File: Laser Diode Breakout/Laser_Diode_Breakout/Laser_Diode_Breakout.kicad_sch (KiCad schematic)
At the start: 3 parts, among them J1 Conn_01x03_Pin

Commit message: generated BOM
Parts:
- D1: value LED -> 785nm Laser Diode
- D2: value LED -> 520nm Laser Diode
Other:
- moved on the sheet: D1, D2, J1

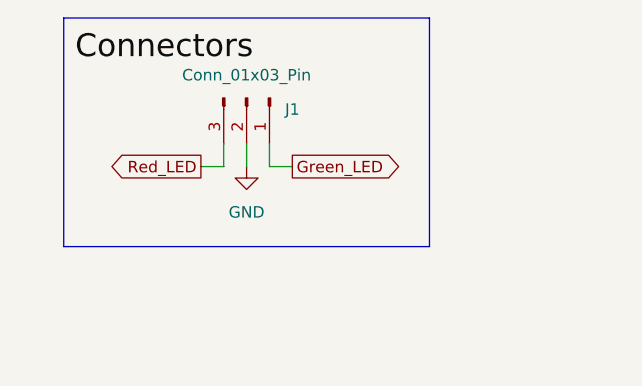
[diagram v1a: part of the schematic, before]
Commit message: fix: switched connectors to Molex
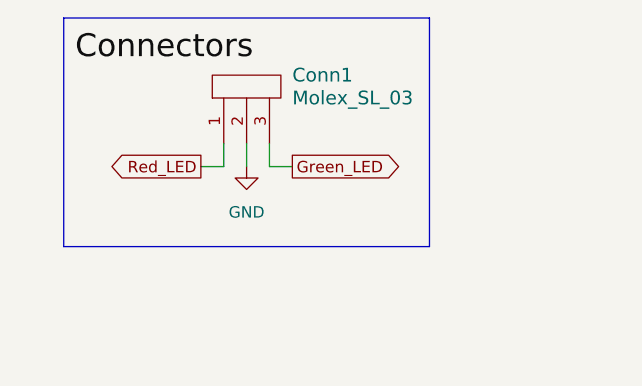
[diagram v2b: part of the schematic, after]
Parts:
- removed J1: Conn_01x03_Pin, symbol Connector:Conn_01x03_Pin
- added Conn1: Molex_SL_03, symbol MRDT_Connectors:Molex_SL_03
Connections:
- net GND: now also Conn1.2
- net Green_LED: now also Conn1.3
- net Red_LED: now also Conn1.1
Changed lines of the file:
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@@
+    )
+  )
+  (symbol (lib_id "MRDT_Connectors:Molex_SL_03") (at 57.15 26.67 90) (unit 1)
+    (in_bom yes) (on_board yes) (dnp no) (fields_autoplaced)
+    (property "Reference" "Conn1" (at 58.42 24.13 90)
+      (effects (font (size 1.524 1.524)) (justify right))
+    )
+    (property "Value" "Molex_SL_03" (at 58.42 26.67 90)
+      (effects (font (size 1.524 1.524)) (justify right))
+    )
+    (property "Footprint" "" (at 57.15 26.67 0)
+      (effects (font (size 1.524 1.524)) hide)
+    )
+    (property "Datasheet" "" (at 57.15 26.67 0)
+      (effects (font (size 1.524 1.524)) hide)
+    )
+    (pin "1")
+    (pin "2")
+    (pin "3")
+    (instances
+      (project "Laser_Diode_Breakout"
+        (path "/c855c228-4e5d-4dfd-9922-c2d1c9f93d6f"
+          (reference "Conn1") (unit 1)
+        )
+      )
     )
   )
@@
         )
       )
-    )
-  )
-  (symbol (lib_id "Connector:Conn_01x03_Pin") (at 53.34 26.67 270) (unit 1)
-    (in_bom yes) (on_board yes) (dnp no)
-    (property "Reference" "J1" (at 58.42 27.94 90)
-      (effects (font (size 1.27 1.27)))
-    )
-    (property "Value" "Conn_01x03_Pin" (at 53.34 24.13 90)
-      (effects (font (size 1.27 1.27)))
-    )
-    (property "Footprint" "" (at 53.34 26.67 0)
-      (effects (font (size 1.27 1.27)) hide)
-    )
-    (property "Datasheet" "~" (at 53.34 26.67 0)
-      (effects (font (size 1.27 1.27)) hide)
-    )
-    (pin "1")
-    (pin "2")
-    (pin "3")
-    (instances
-      (project "Laser_Diode_Breakout"
-        (path "/c855c228-4e5d-4dfd-9922-c2d1c9f93d6f"
-          (reference "J1") (unit 1)
-        )
-      )

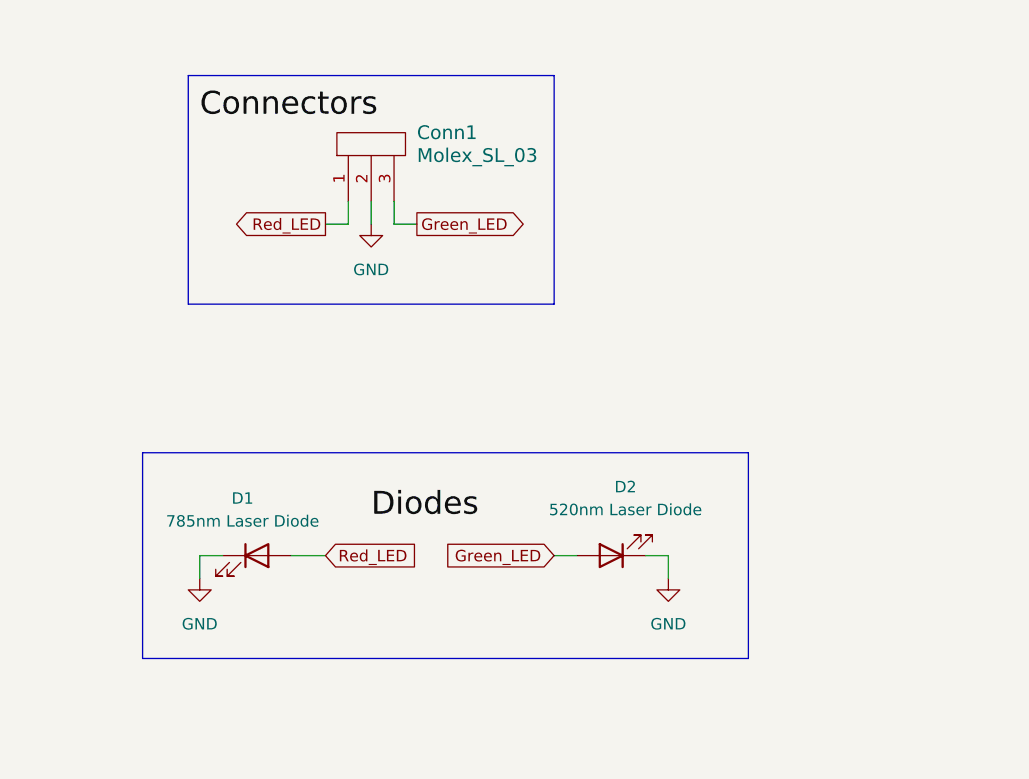
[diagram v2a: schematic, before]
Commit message: fix: replaced net labels with text
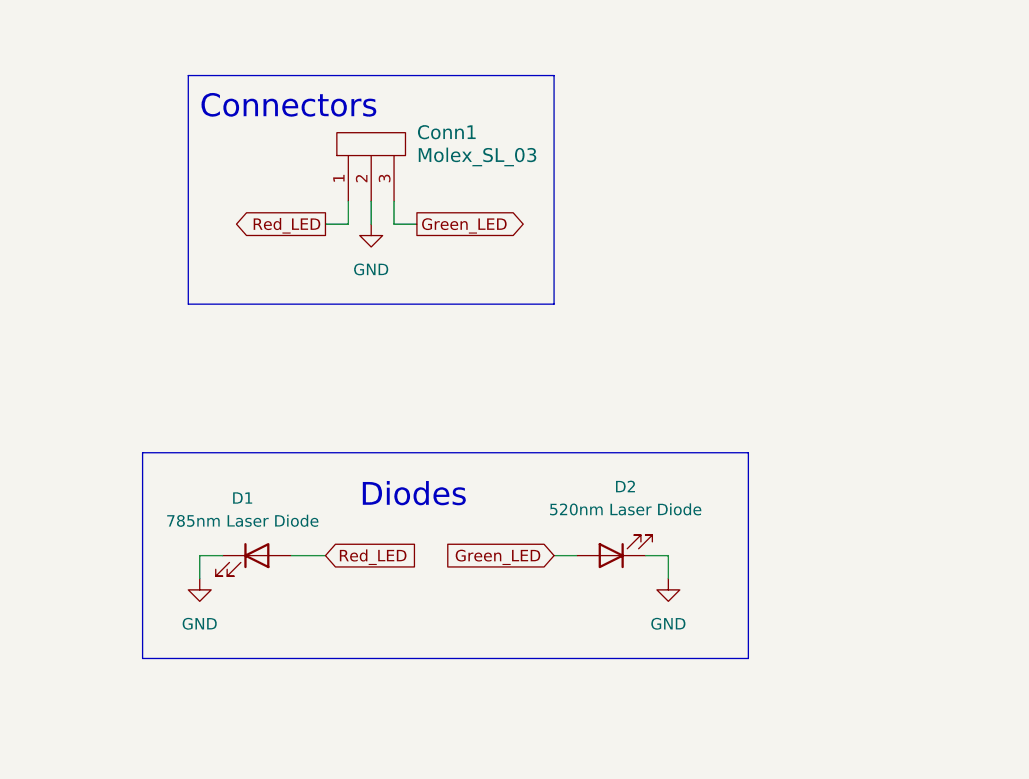
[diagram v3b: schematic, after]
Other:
- note added: "Connectors"
- note added: "Diodes"
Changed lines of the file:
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@@
     (stroke (width 0) (type default))
   )
-  (label "Diodes" (at 53.34 67.31 0) (fields_autoplaced)
+  (text "Connectors" (at 34.29 22.86 0)
     (effects (font (size 2.54 2.54)) (justify left bottom))
   )
-  (label "Connectors" (at 34.29 22.86 0) (fields_autoplaced)
+  (text "Diodes" (at 52.07 66.04 0)
     (effects (font (size 2.54 2.54)) (justify left bottom))
   )

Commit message: misc schematic review changes
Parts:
- added R1: 17, symbol Device:R
- added R2: 24, symbol Device:R
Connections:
- net Green_LED: now also R1.1; no longer D2.2 (A)
- net Red_LED: now also R2.2; no longer D1.2 (A)
- new net: D2.2 (A), R1.2
- new net: D1.2 (A), R2.1
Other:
- moved on the sheet: D2
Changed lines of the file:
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@@
     (stroke (width 0) (type default))
   )
-  (polyline (pts (xy 95.25 82.55) (xy 27.94 82.55))
+  (polyline (pts (xy 124.46 83.82) (xy 27.94 83.82))
     (stroke (width 0) (type default))
   )
@@
     (stroke (width 0) (type default))
   )
-  (polyline (pts (xy 95.25 59.69) (xy 95.25 82.55))
+  (polyline (pts (xy 124.46 60.96) (xy 124.46 83.82))
     (stroke (width 0) (type default))
   )
@@
     (stroke (width 0) (type default))
   )
-  (polyline (pts (xy 27.94 59.69) (xy 95.25 59.69))
+  (polyline (pts (xy 27.94 60.96) (xy 124.46 60.96))
     (stroke (width 0) (type default))
   )
@@
     (stroke (width 0) (type default))
   )
-  (wire (pts (xy 44.45 71.12) (xy 48.26 71.12))
+  (wire (pts (xy 58.42 71.12) (xy 62.23 71.12))
+    (stroke (width 0) (type default))
+  )
+  (wire (pts (xy 44.45 71.12) (xy 50.8 71.12))
     (stroke (width 0) (type default))
   )
@@
     (stroke (width 0) (type default))
   )
-  (wire (pts (xy 86.36 71.12) (xy 86.36 73.66))
-    (stroke (width 0) (type default))
-  )
-  (wire (pts (xy 73.66 71.12) (xy 76.2 71.12))
+  (wire (pts (xy 116.84 72.39) (xy 116.84 74.93))
+    (stroke (width 0) (type default))
+  )
+  (wire (pts (xy 92.71 72.39) (xy 95.25 72.39))
     (stroke (width 0) (type default))
   )
@@
     (stroke (width 0) (type default))
   )
+  (wire (pts (xy 102.87 72.39) (xy 106.68 72.39))
+    (stroke (width 0) (type default))
+  )
   (wire (pts (xy 55.88 31.75) (xy 55.88 34.29))
     (stroke (width 0) (type default))
@@
     (stroke (width 0) (type default))
   )
-  (wire (pts (xy 83.82 71.12) (xy 86.36 71.12))
+  (wire (pts (xy 114.3 72.39) (xy 116.84 72.39))
     (stroke (width 0) (type default))
   )
@@
     )
   )
-  (global_label "Red_LED" (shape input) (at 48.26 71.12 0) (fields_autoplaced)
+  (global_label "Red_LED" (shape input) (at 62.23 71.12 0) (fields_autoplaced)
     (effects (font (size 1.27 1.27)) (justify left))
-    (property "Intersheetrefs" "${INTERSHEET_REFS}" (at 59.1675 71.12 0)
+    (property "Intersheetrefs" "${INTERSHEET_REFS}" (at 73.1375 71.12 0)
       (effects (font (size 1.27 1.27)) (justify left) hide)
     )
   )
-  (global_label "Green_LED" (shape input) (at 73.66 71.12 180) (fields_autoplaced)
+  (global_label "Green_LED" (shape input) (at 92.71 72.39 180) (fields_autoplaced)
     (effects (font (size 1.27 1.27)) (justify right))
-    (property "Intersheetrefs" "${INTERSHEET_REFS}" (at 60.8777 71.12 0)
+    (property "Intersheetrefs" "${INTERSHEET_REFS}" (at 79.9277 72.39 0)
       (effects (font (size 1.27 1.27)) (justify right) hide)
     )
   )
-  (symbol (lib_id "Device:LED") (at 80.01 71.12 180) (unit 1)
+  (symbol (lib_id "Device:LED") (at 110.49 72.39 180) (unit 1)
     (in_bom yes) (on_board yes) (dnp no)
-    (property "Reference" "D2" (at 81.5975 63.5 0)
-      (effects (font (size 1.27 1.27)))
-    )
-    (property "Value" "520nm Laser Diode" (at 81.5975 66.04 0)
-      (effects (font (size 1.27 1.27)))
-    )
-    (property "Footprint" "" (at 80.01 71.12 0)
-      (effects (font (size 1.27 1.27)) hide)
-    )
-    (property "Datasheet" "~" (at 80.01 71.12 0)
+    (property "Reference" "D2" (at 112.0775 64.77 0)
+      (effects (font (size 1.27 1.27)))
+    )
+    (property "Value" "520nm Laser Diode" (at 112.0775 67.31 0)
+      (effects (font (size 1.27 1.27)))
+    )
+    (property "Footprint" "" (at 110.49 72.39 0)
+      (effects (font (size 1.27 1.27)) hide)
+    )
+    (property "Datasheet" "~" (at 110.49 72.39 0)
       (effects (font (size 1.27 1.27)) hide)
     )
@@
     )
   )
-  (symbol (lib_id "power:GND") (at 86.36 73.66 0) (unit 1)
-    (in_bom yes) (on_board yes) (dnp no) (fields_autoplaced)
-    (property "Reference" "#PWR01" (at 86.36 80.01 0)
-      (effects (font (size 1.27 1.27)) hide)
-    )
-    (property "Value" "GND" (at 86.36 78.74 0)
-      (effects (font (size 1.27 1.27)))
-    )
-    (property "Footprint" "" (at 86.36 73.66 0)
-      (effects (font (size 1.27 1.27)) hide)
-    )
-    (property "Datasheet" "" (at 86.36 73.66 0)
+  (symbol (lib_id "Device:R") (at 99.06 72.39 90) (unit 1)
+    (in_bom yes) (on_board yes) (dnp no)
+    (property "Reference" "R1" (at 99.06 69.85 90)
+      (effects (font (size 1.27 1.27)))
+    )
+    (property "Value" "17" (at 99.06 72.39 90)
+      (effects (font (size 1.27 1.27)))
+    )
+    (property "Footprint" "" (at 99.06 74.168 90)
+      (effects (font (size 1.27 1.27)) hide)
+    )
+    (property "Datasheet" "~" (at 99.06 72.39 0)
+      (effects (font (size 1.27 1.27)) hide)
+    )
+    (pin "1")
+    (pin "2")
+    (instances
+      (project "Laser_Diode_Breakout"
+        (path "/c855c228-4e5d-4dfd-9922-c2d1c9f93d6f"
+          (reference "R1") (unit 1)
+        )
+      )
+      (project "Raman_Spectrometer_Board"
+        (path "/dd57774e-6364-4f58-a24d-9970470de2f9"
+          (reference "R3") (unit 1)
+        )
+      )
+    )
+  )
+  (symbol (lib_id "power:GND") (at 116.84 74.93 0) (unit 1)
+    (in_bom yes) (on_board yes) (dnp no) (fields_autoplaced)
+    (property "Reference" "#PWR01" (at 116.84 81.28 0)
+      (effects (font (size 1.27 1.27)) hide)
+    )
+    (property "Value" "GND" (at 116.84 80.01 0)
+      (effects (font (size 1.27 1.27)))
+    )
+    (property "Footprint" "" (at 116.84 74.93 0)
+      (effects (font (size 1.27 1.27)) hide)
+    )
+    (property "Datasheet" "" (at 116.84 74.93 0)
       (effects (font (size 1.27 1.27)) hide)
     )
@@
         )
       )
+    )
+  )
+  (symbol (lib_id "Device:R") (at 54.61 71.12 90) (unit 1)
+    (in_bom yes) (on_board yes) (dnp no)
+    (property "Reference" "R2" (at 54.61 68.58 90)
+      (effects (font (size 1.27 1.27)))
+    )
+    (property "Value" "24" (at 54.61 71.12 90)
+      (effects (font (size 1.27 1.27)))
+    )
+    (property "Footprint" "" (at 54.61 72.898 90)
+      (effects (font (size 1.27 1.27)) hide)
+    )
+    (property "Datasheet" "~" (at 54.61 71.12 0)
+      (effects (font (size 1.27 1.27)) hide)
+    )
+    (pin "1")
+    (pin "2")
+    (instances
+      (project "Laser_Diode_Breakout"
+        (path "/c855c228-4e5d-4dfd-9922-c2d1c9f93d6f"
+          (reference "R2") (unit 1)
+        )
+      )
+      (project "Raman_Spectrometer_Board"
+        (path "/dd57774e-6364-4f58-a24d-9970470de2f9"
+          (reference "R4") (unit 1)
+        )
+      )

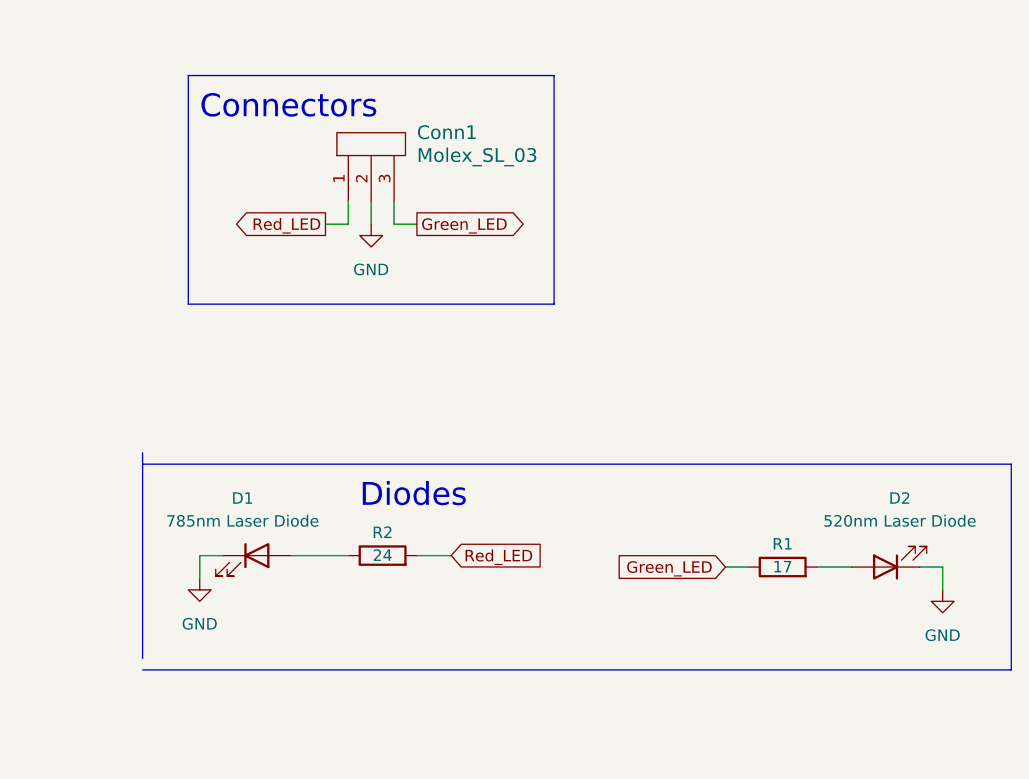
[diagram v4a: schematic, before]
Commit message: fix: use mosfets to control diodes
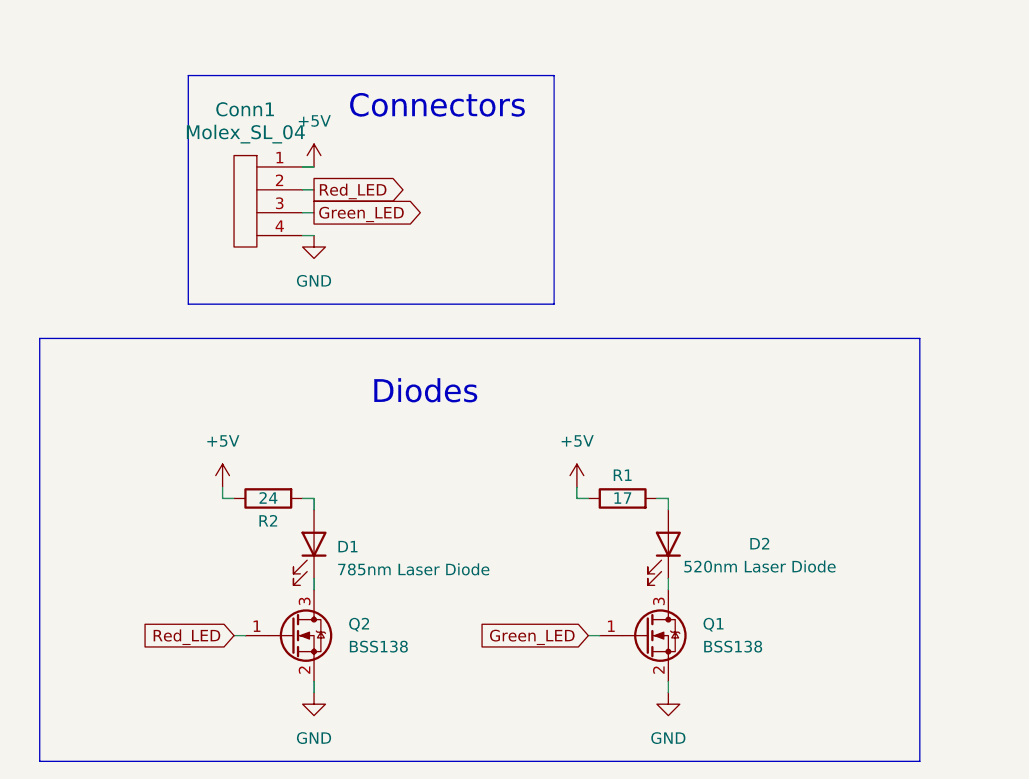
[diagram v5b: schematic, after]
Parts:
- removed Conn1: Molex_SL_03, symbol MRDT_Connectors:Molex_SL_03
- added Conn1: Molex_SL_04, symbol MRDT_Connectors:Molex_SL_04
- added Q1, Q2: BSS138, Package_TO_SOT_SMD:SOT-23, symbol Transistor_FET:BSS138
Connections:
- net GND: now also Conn1.4, Q1.2 (S), Q2.2 (S); no longer D1.1 (K), D2.1 (K)
- net Green_LED: now also Conn1.3, Q1.1 (G); no longer R1.1
- net Red_LED: now also Conn1.2, Q2.1 (G); no longer R2.2
- net at D1.2 (A): now also R2.2; no longer R2.1
- new net: D2.1 (K), Q1.3 (D)
- new net: D1.1 (K), Q2.3 (D)
- new net +5V: Conn1.1, R1.1, R2.1
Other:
- moved on the sheet: D2, R1

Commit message: //WIP working on fixing diodes
we though one of the diodes required 2V, but that was its reverse voltage. It actually wants 5.9, so we need to change the diode board to account
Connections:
- net +5V renamed +12V
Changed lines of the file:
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@@
-    )
-  )
-  (symbol (lib_id "power:+5V") (at 46.99 27.94 0) (unit 1)
-    (in_bom yes) (on_board yes) (dnp no) (fields_autoplaced)
-    (property "Reference" "#PWR04" (at 46.99 31.75 0)
-      (effects (font (size 1.27 1.27)) hide)
-    )
-    (property "Value" "+5V" (at 46.99 22.86 0)
-      (effects (font (size 1.27 1.27)))
-    )
-    (property "Footprint" "" (at 46.99 27.94 0)
-      (effects (font (size 1.27 1.27)) hide)
-    )
-    (property "Datasheet" "" (at 46.99 27.94 0)
-      (effects (font (size 1.27 1.27)) hide)
-    )
-    (pin "1")
-    (instances
-      (project "Laser_Diode_Breakout"
-        (path "/c855c228-4e5d-4dfd-9922-c2d1c9f93d6f"
-          (reference "#PWR04") (unit 1)
-        )
-      )
-    )
-  )
-  (symbol (lib_id "power:+5V") (at 36.83 63.5 0) (unit 1)
-    (in_bom yes) (on_board yes) (dnp no) (fields_autoplaced)
-    (property "Reference" "#PWR07" (at 36.83 67.31 0)
-      (effects (font (size 1.27 1.27)) hide)
-    )
-    (property "Value" "+5V" (at 36.83 58.42 0)
-      (effects (font (size 1.27 1.27)))
-    )
-    (property "Footprint" "" (at 36.83 63.5 0)
-      (effects (font (size 1.27 1.27)) hide)
-    )
-    (property "Datasheet" "" (at 36.83 63.5 0)
-      (effects (font (size 1.27 1.27)) hide)
-    )
-    (pin "1")
-    (instances
-      (project "Laser_Diode_Breakout"
-        (path "/c855c228-4e5d-4dfd-9922-c2d1c9f93d6f"
-          (reference "#PWR07") (unit 1)
-        )
-      )
     )
   )
@@
     )
   )
+  (symbol (lib_id "power:+12V") (at 76.2 63.5 0) (unit 1)
+    (in_bom yes) (on_board yes) (dnp no) (fields_autoplaced)
+    (property "Reference" "#PWR04" (at 76.2 67.31 0)
+      (effects (font (size 1.27 1.27)) hide)
+    )
+    (property "Value" "+12V" (at 76.2 58.42 0)
+      (effects (font (size 1.27 1.27)))
+    )
+    (property "Footprint" "" (at 76.2 63.5 0)
+      (effects (font (size 1.27 1.27)) hide)
+    )
+    (property "Datasheet" "" (at 76.2 63.5 0)
+      (effects (font (size 1.27 1.27)) hide)
+    )
+    (pin "1")
+    (instances
+      (project "Laser_Diode_Breakout"
+        (path "/c855c228-4e5d-4dfd-9922-c2d1c9f93d6f"
+          (reference "#PWR04") (unit 1)
+        )
+      )
+    )
+  )
   (symbol (lib_id "power:GND") (at 46.99 35.56 0) (unit 1)
     (in_bom yes) (on_board yes) (dnp no) (fields_autoplaced)
@@
         (path "/c855c228-4e5d-4dfd-9922-c2d1c9f93d6f"
           (reference "Conn1") (unit 1)
+        )
+      )
+    )
+  )
+  (symbol (lib_id "power:+12V") (at 36.83 63.5 0) (unit 1)
+    (in_bom yes) (on_board yes) (dnp no) (fields_autoplaced)
+    (property "Reference" "#PWR02" (at 36.83 67.31 0)
+      (effects (font (size 1.27 1.27)) hide)
+    )
+    (property "Value" "+12V" (at 36.83 58.42 0)
+      (effects (font (size 1.27 1.27)))
+    )
+    (property "Footprint" "" (at 36.83 63.5 0)
+      (effects (font (size 1.27 1.27)) hide)
+    )
+    (property "Datasheet" "" (at 36.83 63.5 0)
+      (effects (font (size 1.27 1.27)) hide)
+    )
+    (pin "1")
+    (instances
+      (project "Laser_Diode_Breakout"
+        (path "/c855c228-4e5d-4dfd-9922-c2d1c9f93d6f"
+          (reference "#PWR02") (unit 1)
+        )
+      )
+    )
+  )
+  (symbol (lib_id "power:+12V") (at 46.99 27.94 0) (unit 1)
+    (in_bom yes) (on_board yes) (dnp no) (fields_autoplaced)
+    (property "Reference" "#PWR01" (at 46.99 31.75 0)
+      (effects (font (size 1.27 1.27)) hide)
+    )
+    (property "Value" "+12V" (at 46.99 22.86 0)
+      (effects (font (size 1.27 1.27)))
+    )
+    (property "Footprint" "" (at 46.99 27.94 0)
+      (effects (font (size 1.27 1.27)) hide)
+    )
+    (property "Datasheet" "" (at 46.99 27.94 0)
+      (effects (font (size 1.27 1.27)) hide)
+    )
+    (pin "1")
+    (instances
+      (project "Laser_Diode_Breakout"
+        (path "/c855c228-4e5d-4dfd-9922-c2d1c9f93d6f"
+          (reference "#PWR01") (unit 1)
         )
       )
@@
         )
       )
-    )
-  )
-  (symbol (lib_id "power:+5V") (at 76.2 63.5 0) (unit 1)
-    (in_bom yes) (on_board yes) (dnp no) (fields_autoplaced)
-    (property "Reference" "#PWR08" (at 76.2 67.31 0)
-      (effects (font (size 1.27 1.27)) hide)
-    )
-    (property "Value" "+5V" (at 76.2 58.42 0)
-      (effects (font (size 1.27 1.27)))
-    )
-    (property "Footprint" "" (at 76.2 63.5 0)
-      (effects (font (size 1.27 1.27)) hide)
-    )
-    (property "Datasheet" "" (at 76.2 63.5 0)
-      (effects (font (size 1.27 1.27)) hide)
-    )
-    (pin "1")
-    (instances
-      (project "Laser_Diode_Breakout"
-        (path "/c855c228-4e5d-4dfd-9922-c2d1c9f93d6f"
-          (reference "#PWR08") (unit 1)
-        )
-      )

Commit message: fixed resitor values on diode board
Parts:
- R1: value 17 -> 33
- R2: value 24 -> 78.7
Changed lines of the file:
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@@
       (effects (font (size 1.27 1.27)))
     )
-    (property "Value" "17" (at 81.28 64.77 90)
+    (property "Value" "33" (at 81.28 64.77 90)
       (effects (font (size 1.27 1.27)))
     )
@@
       (effects (font (size 1.27 1.27)))
     )
-    (property "Value" "24" (at 41.91 64.77 90)
+    (property "Value" "78.7" (at 41.91 64.77 90)
       (effects (font (size 1.27 1.27)))
     )
